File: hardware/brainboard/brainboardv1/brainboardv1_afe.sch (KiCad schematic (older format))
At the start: 29 parts, among them P10 CONN_2X2, U3 OPA2376, U4 ADS1299

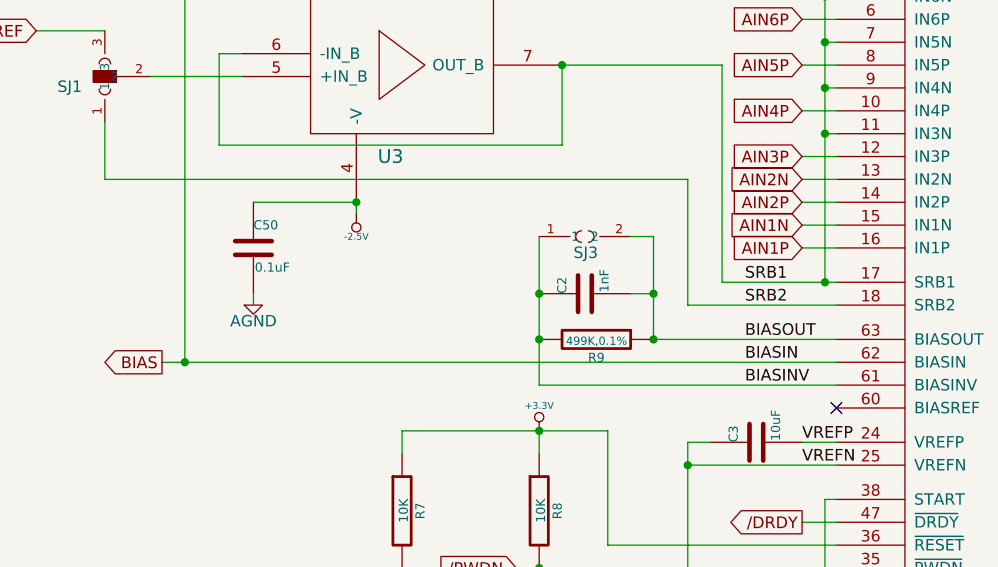
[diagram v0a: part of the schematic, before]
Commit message: Thesis version
Finally able to commit again (Windows XP issues fixed by OS upgrade).
Added latest version of wearable BB, along with prototype "muscleboard"
2-channel board for EMG/ECG applications
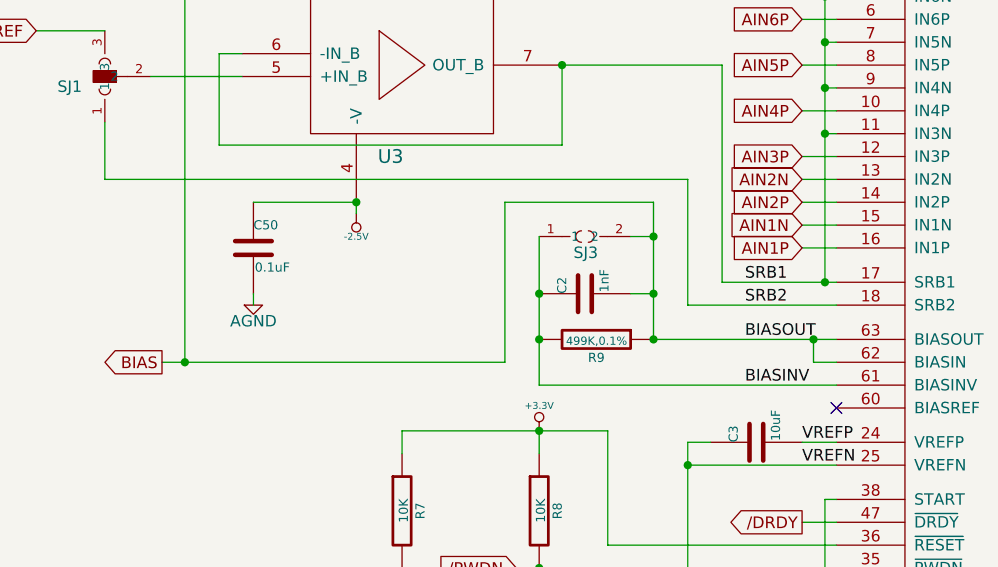
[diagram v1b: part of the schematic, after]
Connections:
- net BIASOUT is gone; now on net BIAS: C2.2, R9.1, SJ3.2, U4.63 (BIASOUT)
